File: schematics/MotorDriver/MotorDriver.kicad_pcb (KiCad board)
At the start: 2 copper layers, 13 parts, among them J1 I2C, J2 UART, J3 3V3IN, J4 9VIN, U1 ATmega328P-PU, U2 TB6612FNG, Y1 16MHz

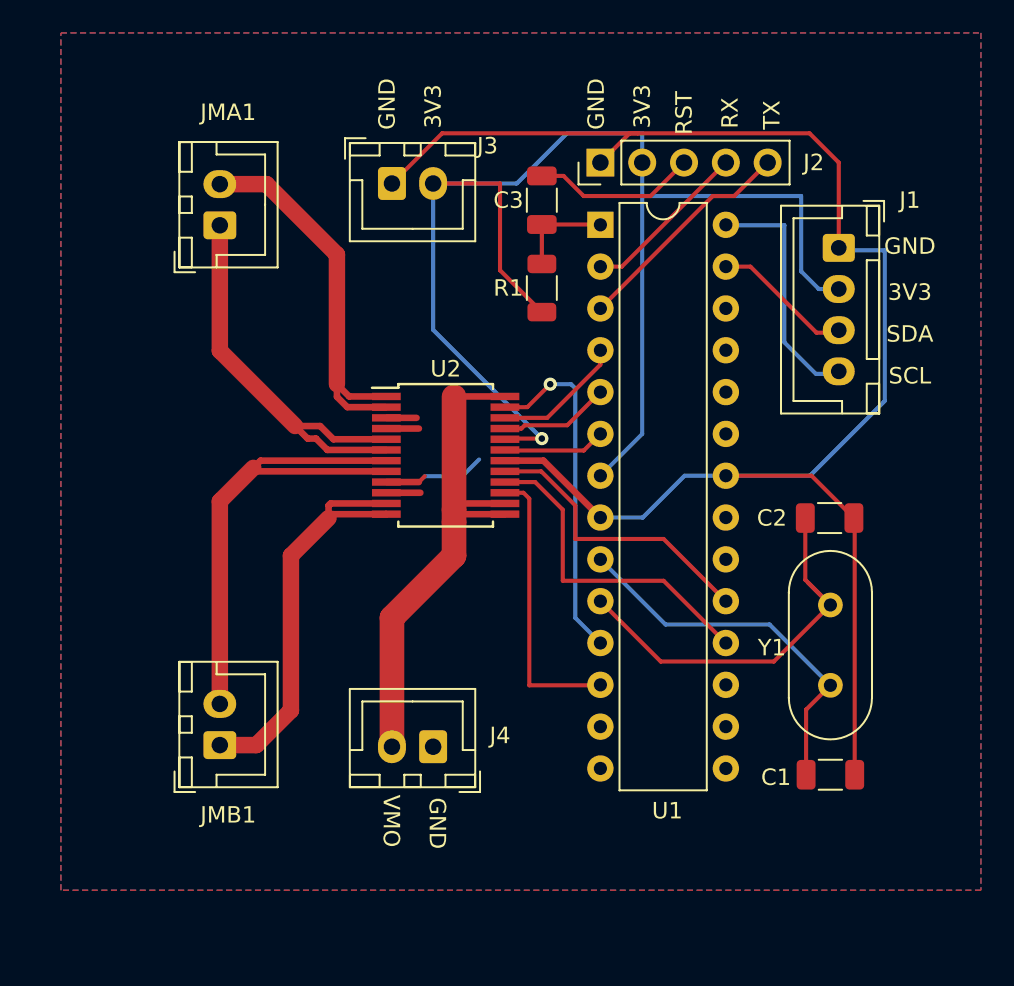
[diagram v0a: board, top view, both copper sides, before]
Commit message: Added Caps
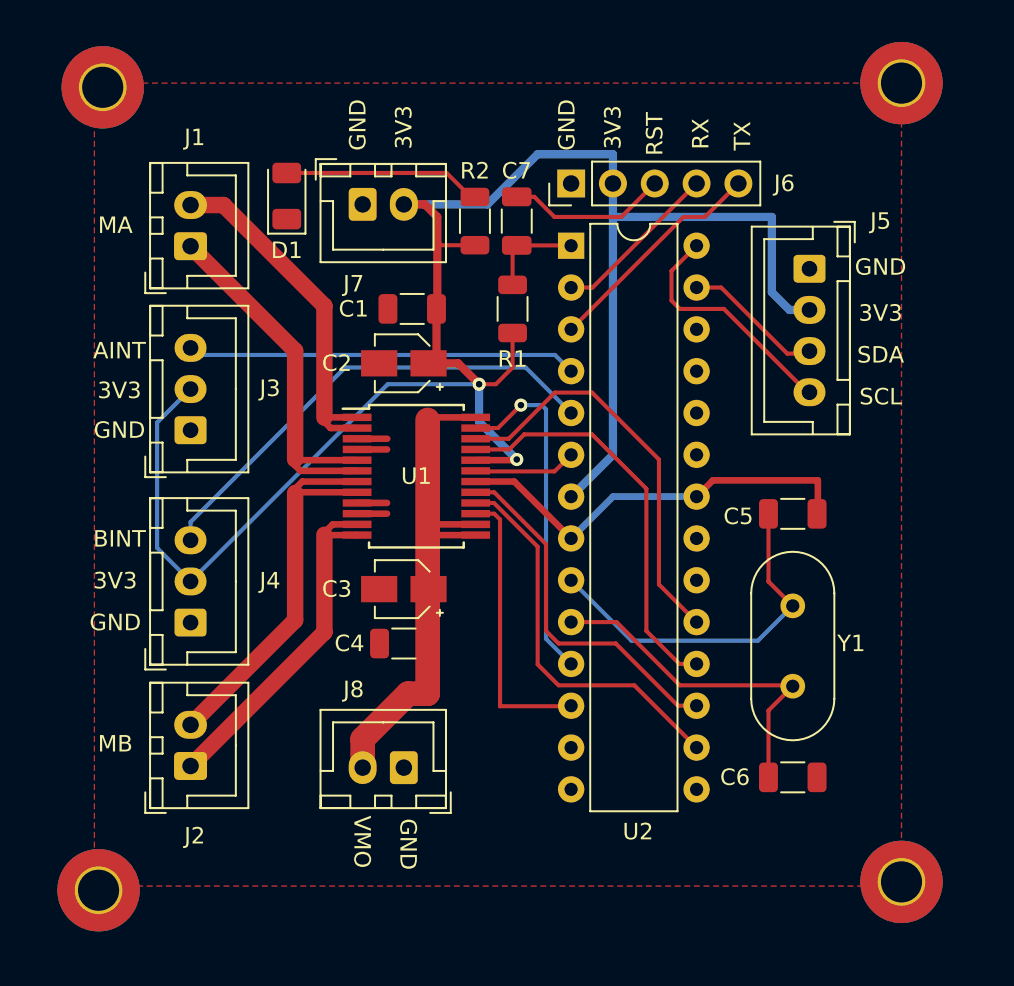
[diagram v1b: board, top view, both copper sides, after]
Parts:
- added C1: 0.1uf, Capacitor_SMD:C_1206_3216Metric, F.Cu at (72.1, 73.7)
- added C2: 10uf, Capacitor_SMD:CP_Elec_3x5.3, F.Cu at (71.6, 77.0)
- added C3: 10uf, Capacitor_SMD:CP_Elec_3x5.3, F.Cu at (71.6, 90.7)
- added C4: 0.1uf, Capacitor_SMD:C_1206_3216Metric, F.Cu at (71.6, 94.0)
- added D1: LED, LED_SMD:LED_1206_3216Metric, F.Cu at (64.5, 66.8)
- added H1: MountingHole, MountingHole:MountingHole_2.5mm_Pad_TopBottom, F.Cu at (53.3, 60.2)
- added H2: MountingHole, MountingHole:MountingHole_2.5mm_Pad_TopBottom, F.Cu at (53.1, 109.0)
- added H3: MountingHole, MountingHole:MountingHole_2.5mm_Pad_TopBottom, F.Cu at (101.9, 59.9)
- added H4: MountingHole, MountingHole:MountingHole_2.5mm_Pad_TopBottom, F.Cu at (101.9, 108.5)
- added J3: MENCA, Connector_JST:JST_XH_B3B-XH-A_1x03_P2.50mm_Vertical, F.Cu at (58.7, 81.0)
- added J4: MENCB, Connector_JST:JST_XH_B3B-XH-A_1x03_P2.50mm_Vertical, F.Cu at (58.7, 92.7)
- added R2: 330, Resistor_SMD:R_1206_3216Metric, F.Cu at (75.9, 68.3)
- moved C5 16.0 mm to (95.2, 86.1)
- moved C6 15.9 mm to (95.2, 102.1)
- moved Y1 5.34 mm to (95.2, 91.7), turned to 270 degrees
- moved J6 2.18 mm to (81.8, 66.0)
- moved J7 2.18 mm to (69.1, 67.3)
- moved J8 2.18 mm to (71.6, 101.5)
- moved R1 2.18 mm to (78.2, 73.7)
- moved U1 2.18 mm to (72.4, 83.8)
- moved U2 2.18 mm to (81.8, 69.8)
- moved J1 2.18 mm to (58.7, 69.8)
- moved J2 2.18 mm to (58.7, 101.4)
- moved J5 2.18 mm to (96.3, 71.2)
- moved C7 1.98 mm to (78.5, 68.3)
- renumbered C1 to C5, C2 to C6, C3 to C7, JMA1 to J1, JMB1 to J2, J1 to J5, J2 to J6, J3 to J7, J4 to J8, U2 to U1, U1 to U2
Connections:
- U2 pad 16: (no net) -> /BIN2
- U2 pad 17: (no net) -> /BIN1
- U2 pad 18: /BIN2 -> /AIN1
- U2 pad 19: /BIN1 -> /AIN2
- U2 pad 4: /AIN2 -> /INT0
- U2 pad 5: /AIN1 -> /INT1
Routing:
- net GND: track 113.3 -> 33.1 mm
- net +3V3: track 86.6 -> 118.8 mm, vias 1 -> 2
- net /INT1: track 0.00 -> 29.3 mm
- net /INT0: track 0.00 -> 23.7 mm
- net /AIN1: track 6.72 -> 24.6 mm
- net /AIN2: track 8.25 -> 25.0 mm
- net Net-(D1-Pad2): track 0.00 -> 11.8 mm
- net Net-(J2-Pad2): track 31.6 -> 24.6 mm
- net Net-(J2-Pad1): track 25.8 -> 21.8 mm
- net /BIN1: track 17.9 -> 21.9 mm
- net /BIN2: track 20.0 -> 23.8 mm
- net Net-(C6-Pad1): track 24.7 -> 21.2 mm
- net Net-(J1-Pad1): track 26.1 -> 23.6 mm
- net Net-(J1-Pad2): track 24.1 -> 21.9 mm
- net Net-(C5-Pad1): track 23.2 -> 22.1 mm
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- removed copper zone on B.Cu, net GND
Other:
- board text added: "AINT"
- board text added: "BINT"
- board text added: "MA"
- board text added: "MB"

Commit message: Changes
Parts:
- added C2: 100n, Capacitor_SMD:C_1206_3216Metric, F.Cu at (78.2, 76.2)
- D1: value LED -> RED
- moved R1 1.83 mm to (77.2, 72.1), turned to 0 degrees
- moved H2 1.51 mm to (51.9, 109.9)
- moved H1 1.47 mm to (51.9, 59.9)
- moved H4 1.44 mm to (101.9, 109.9)
- renumbered C2 to C3, C3 to C4, C4 to C5, C5 to C6, C6 to C7, C7 to C8, J5 to J1, J6 to J2, J8 to J3, J7 to J4, J1 to J5, J2 to J6, J3 to J7, J4 to J8
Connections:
- net Net-(J1-Pad1) renamed /AO2
- net Net-(J1-Pad2) renamed /AO1
- net Net-(J2-Pad1) renamed /BO1
- net Net-(J2-Pad2) renamed /BO2
- U2 pad 20: (no net) -> +3V3
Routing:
- net +3V3: track 118.8 -> 137.8 mm, vias 2 -> 4
- net GND: track 33.1 -> 27.1 mm
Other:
- board outline added: 55.4 x 55.4 mm
